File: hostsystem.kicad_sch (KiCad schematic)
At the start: 78 parts, among them J1001 TC2050, J1002 Conn_01x03_Pin, U1001 AM6231ASGGGAALW, U1002 SN74LVC2G241DCUR, U1003 AT24C32D-STUM-T, X1001 32.768kHz, X1002 25MHz

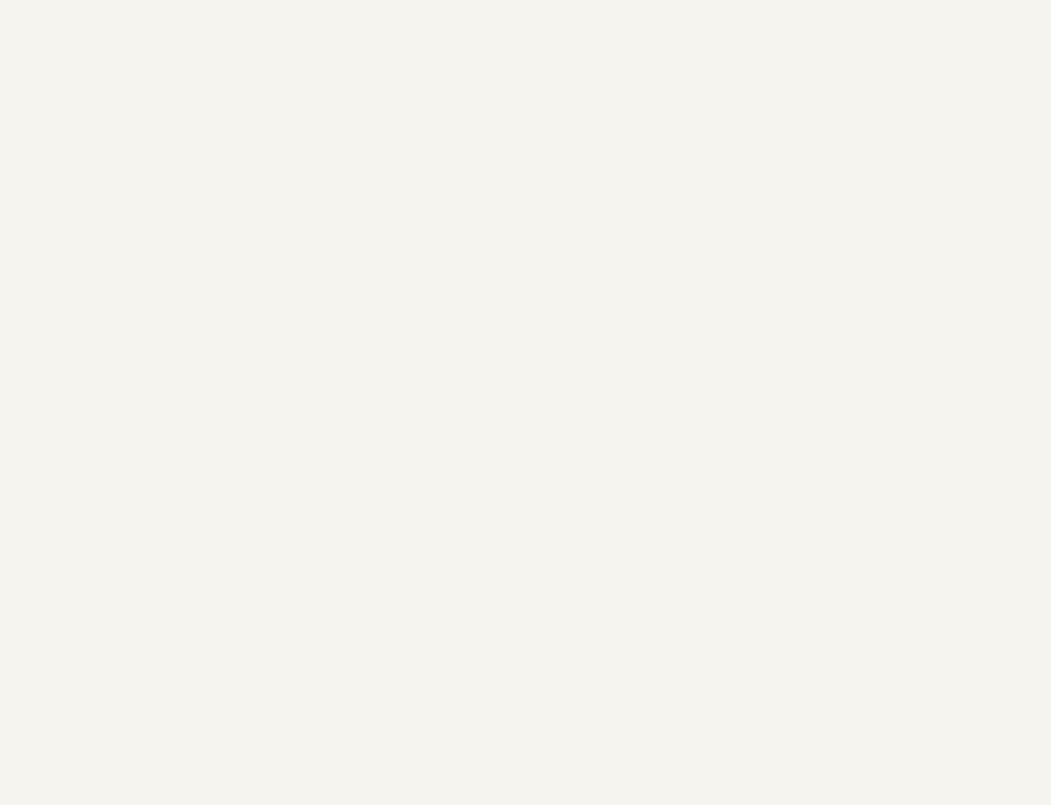
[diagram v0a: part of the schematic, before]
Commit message: Added clock buffor for CMOS 25MHz osc. Used for both SoC and Ethernet with optional SoC crystal still placed
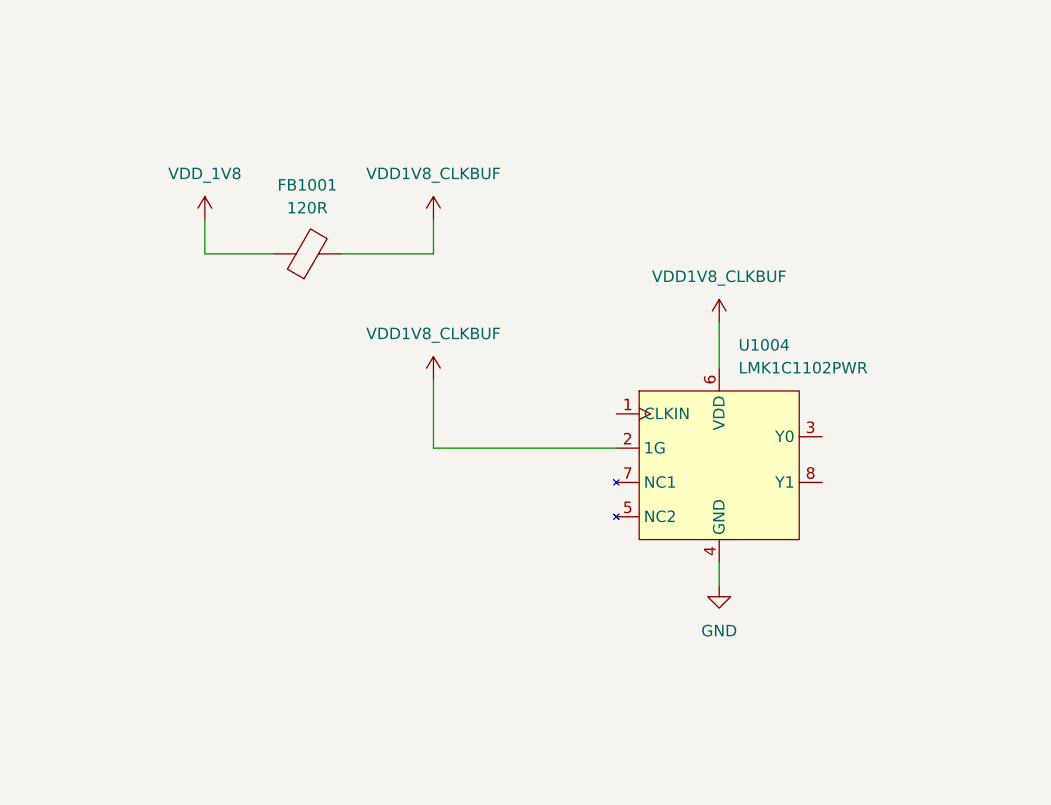
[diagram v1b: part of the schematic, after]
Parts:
- added FB1001: 120R, symbol Device:FerriteBead
- added U1004: LMK1C1102PWR, symbol SoftServicesSymbolLibrary:LMK1C1102PWR
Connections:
- net GND: now also U1004.4 (GND)
- net VDD_1V8: now also FB1001.1
- new net VDD1V8_CLKBUF: FB1001.2, U1004.2 (1G), U1004.6 (VDD)

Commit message: Started USB and OSC routing
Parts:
- removed C1008, C1009: C, Capacitor_SMD:C_0402_1005Metric, symbol Device:C
- removed R1012: 0R, Resistor_SMD:R_0402_1005Metric, symbol Device:R
- added C1010: 0.01u, Capacitor_SMD:C_0201_0603Metric, symbol Device:C
- added C1011: 1u, symbol Device:C
- added C1012, C1013: 0.1u, symbol Device:C
- added R1015: 10k, symbol Device:R
- added R1056, R1057, R1058: 22R, symbol Device:R
- added R1059, R1060: R, symbol Device:R
- added R1061, R1062: 0R, symbol Device:R
- added X1004: ECS-2520MV-250-CN-TR, ECS-2520MV-250-CN-TR:ECS2520MV250CNTR, symbol SoftServicesSymbolLibrary:ECS-2520MV-250-CN-TR
- U1004: footprint (none) -> LMK1C1102PWR:SOP65P640X120-8N
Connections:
- net MCU_OSC0 is gone; now on net MCU_OSC0_XO: U1001.A3 (MCU_SPI0_OSC0_XO)
- net GND: now also C1010.2, C1011.2, C1012.2, C1013.2, R1062.1, X1004.2 (GND)
- net MCU_OSC0_XI: now also R1059.1, R1061.1; no longer C1004.1, X1002.3
- net MCU_OSC0_XO: now also R1060.1, R1062.2; no longer C1006.1, X1002.1
- net VDD1V8_CLKBUF: now also C1010.1, C1011.1, C1012.1, C1013.1, R1015.1, X1004.1 (EN), X1004.4 (VDD); no longer U1004.2 (1G)
- net CLKOUT: now reaches U1004.1 (CLKIN)
- net CLKOUT: now also R1058.2
- net SoC_CLK_BUF: now reaches U1004.3 (Y0)
- net SoC_CLK_BUF: now also R1056.1
- net ETH_CLK_BUF: now reaches U1004.8 (Y1)
- net ETH_CLK_BUF: now also R1057.1
- new net: C1004.1, R1059.2, X1002.3
- new net: C1006.1, R1060.2, X1002.1
- new net CLKBUF_1G: R1015.2, U1004.2 (1G)
- new net CLKOUT_OSC: R1058.1, X1004.3 (OUT)
- new net ETH_CLK: R1057.2
- new net SoC_CLKIN: R1056.2, R1061.2
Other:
- moved on the sheet: C1004, C1006, U1004, X1002

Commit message: Routed most of Ethernet PHY and RGMII
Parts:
- R1015, R1056, R1057, R1058: footprint (none) -> Resistor_SMD:R_0201_0603Metric
- R1061, R1062: footprint (none) -> Resistor_SMD:R_0402_1005Metric
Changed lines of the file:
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@@
 			)
 		)
-		(property "Footprint" ""
+		(property "Footprint" "Resistor_SMD:R_0402_1005Metric"
 			(at 193.04 208.788 90)
 			(effects
@@
 			)
 		)
-		(property "Footprint" ""
+		(property "Footprint" "Resistor_SMD:R_0201_0603Metric"
 			(at 344.932 124.46 90)
 			(effects
@@
 			)
 		)
-		(property "Footprint" ""
+		(property "Footprint" "Resistor_SMD:R_0201_0603Metric"
 			(at 321.31 131.318 90)
 			(effects
@@
 			)
 		)
-		(property "Footprint" ""
+		(property "Footprint" "Resistor_SMD:R_0201_0603Metric"
 			(at 408.94 135.128 90)
 			(effects
@@
 			)
 		)
-		(property "Footprint" ""
+		(property "Footprint" "Resistor_SMD:R_0402_1005Metric"
 			(at 185.928 254 90)
 			(effects
@@
 			)
 		)
-		(property "Footprint" ""
+		(property "Footprint" "Resistor_SMD:R_0201_0603Metric"
 			(at 408.94 130.048 90)
 			(effects

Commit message: Continued PDN routing
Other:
- note added: "CMOS Oscillator + Clock Buffer"
- moved on the sheet: D1004, D1005, D1006, FB1001, R1016, R1017, R1018, R1019, R1020, R1021, R1022, R1023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

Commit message: Improved clock layout and clock PDN
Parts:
- C1010: footprint Capacitor_SMD:C_0201_0603Metric -> Capacitor_SMD:C_0402_1005Metric
- C1011, C1012, C1013: footprint (none) -> Capacitor_SMD:C_0402_1005Metric
- FB1001: footprint (none) -> Resistor_SMD:R_0402_1005Metric
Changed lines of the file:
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@@
 			)
 		)
-		(property "Footprint" "Capacitor_SMD:C_0201_0603Metric"
+		(property "Footprint" "Capacitor_SMD:C_0402_1005Metric"
 			(at 263.8552 132.08 0)
 			(effects
@@
 			)
 		)
-		(property "Footprint" ""
+		(property "Footprint" "Capacitor_SMD:C_0402_1005Metric"
 			(at 229.5652 154.94 0)
 			(effects
@@
 			)
 		)
-		(property "Footprint" ""
+		(property "Footprint" "Resistor_SMD:R_0402_1005Metric"
 			(at 228.6 130.048 90)
 			(effects
@@
 			)
 		)
-		(property "Footprint" ""
+		(property "Footprint" "Capacitor_SMD:C_0402_1005Metric"
 			(at 215.5952 154.94 0)
 			(effects
@@
 			)
 		)
-		(property "Footprint" ""
+		(property "Footprint" "Capacitor_SMD:C_0402_1005Metric"
 			(at 243.5352 154.94 0)
 			(effects

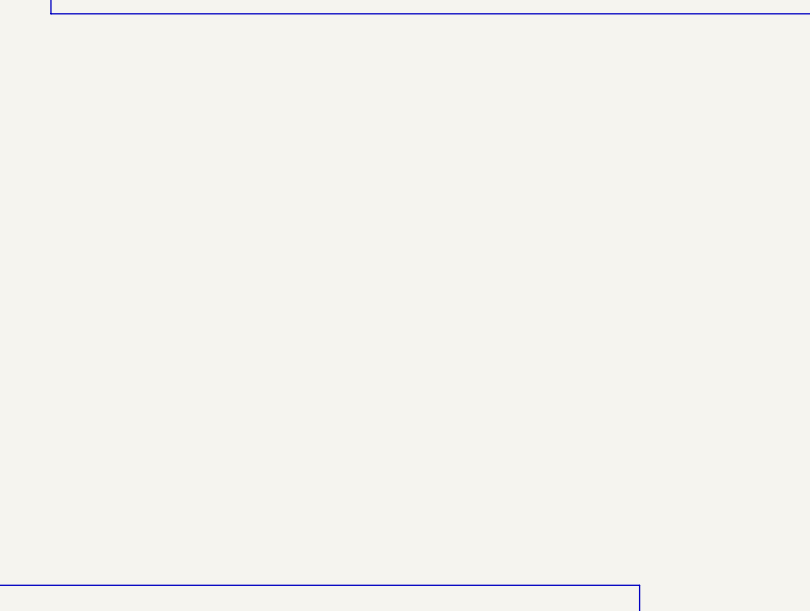
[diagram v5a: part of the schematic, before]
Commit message: Switched out CC2652P and nRF52840 for MGM240P to run Zigbee and Thread
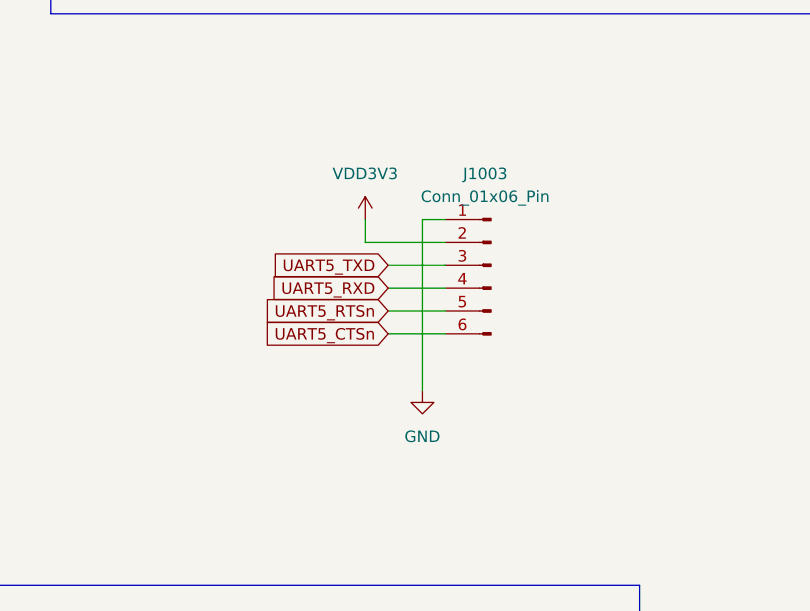
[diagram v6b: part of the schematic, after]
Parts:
- added J1003: Conn_01x06_Pin, Connector_PinHeader_2.54mm:PinHeader_1x06_P2.54mm_Vertical, symbol Connector:Conn_01x06_Pin
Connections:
- net GND: now also J1003.1 (Pin_1)
- net UART5_CTSn: now also J1003.6 (Pin_6)
- net UART5_RTSn: now also J1003.5 (Pin_5)
- net UART5_RXD: now also J1003.4 (Pin_4)
- net UART5_TXD: now also J1003.3 (Pin_3)
- new net VDD3V3: J1003.2 (Pin_2)

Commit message: Added new radio schematic
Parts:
- removed R1054: 100R, symbol Device:R
- removed R1055: 100k, symbol Device:R
- R1046: renamed from R1011; value 33R -> 22R
- R1049: renamed from R1052; value 33R -> 22R
- R1051: renamed from R1053; value 33R -> 22R
- renumbered C1010 to C1001, C1011 to C1002, C1012 to C1003, C1013 to C1004, C1004 to C1005, C1002 to C1007, C1003 to C1008, C1001 to C1009, C1007 to C1010, C1005 to C1011, D1004 to D1001, D1005 to D1002, D1006 to D1003, D1001 to D1004, D1002 to D1005, D1003 to D1006, J1003 to J1001, J1001 to J1002, J1002 to J1003, R1048 to R1001, R1016 to R1002, R1017 to R1003, R1018 to R1004, R1019 to R1005, R1020 to R1006, R1021 to R1007, R1023 to R1008, R1022 to R1009, R1024 to R1010, R1025 to R1011, R1026 to R1012, R1027 to R1013, R1028 to R1014, R1029 to R1015, R1030 to R1016, R1031 to R1017, R1001 to R1018, R1002 to R1019, R1015 to R1020, R1056 to R1021, R1058 to R1022, R1057 to R1023, R1049 to R1024, R1050 to R1025, R1051 to R1026, R1032 to R1027, R1033 to R1028, R1034 to R1029, R1035 to R1030, R1036 to R1031, R1037 to R1032, R1038 to R1033, R1039 to R1034, R1040 to R1035, R1041 to R1036, R1042 to R1037, R1043 to R1038, R1044 to R1039, R1045 to R1040, R1046 to R1041, R1047 to R1042, R1009 to R1043, R1010 to R1044, R1061 to R1045, R1059 to R1047, R1060 to R1052, R1062 to R1053, R1003 to R1054, R1004 to R1055, R1005 to R1056, R1006 to R1057, R1007 to R1058, R1013 to R1059, R1014 to R1060, R1008 to R1061, U1004 to U1001, U1001 to U1002, U1002 to U1003, U1003 to U1004, X1004 to X1001, X1001 to X1003
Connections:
- net CC2652_BOOT: no longer names the net of U1002.F23 (OSPI0_CSN0)
- net CC2652_RSTn: no longer names the net of U1002.G21 (OSPI0_CSN1)
- net CC2652_UART6_CTSn: no longer names the net of U1002.J22 (OSPI0_D7)
- net CC2652_UART6_RTSn: no longer names the net of U1002.H25 (OSPI0_D6)
- net CC2652_UART6_RXD: no longer names the net of U1002.J23 (OSPI0_D4)
- net CC2652_UART6_TXD: no longer names the net of U1002.J25 (OSPI0_D5)
- net nRF_INTn renamed MDM_SPI0_IRQ
- net nRF_SPI0_CLK renamed MGM_SPI0_CLK
- net nRF_SPI0_CS0 renamed MGM_SPI0_CS
- net nRF_SPI0_MISO renamed MGM_SPI0_MISO
- net nRF_SPI0_MOSI renamed MGM_SPI0_MOSI
- net nRF_SoC_CLK renamed MGM_SoC_CLK
- net nRF_SoC_MOSI renamed MGM_SoC_MOSI
- net nRF_SoC_nRESET: no longer names the net of U1002.B15 (UART0_RTSN)
- no-connect marks 103 -> 109

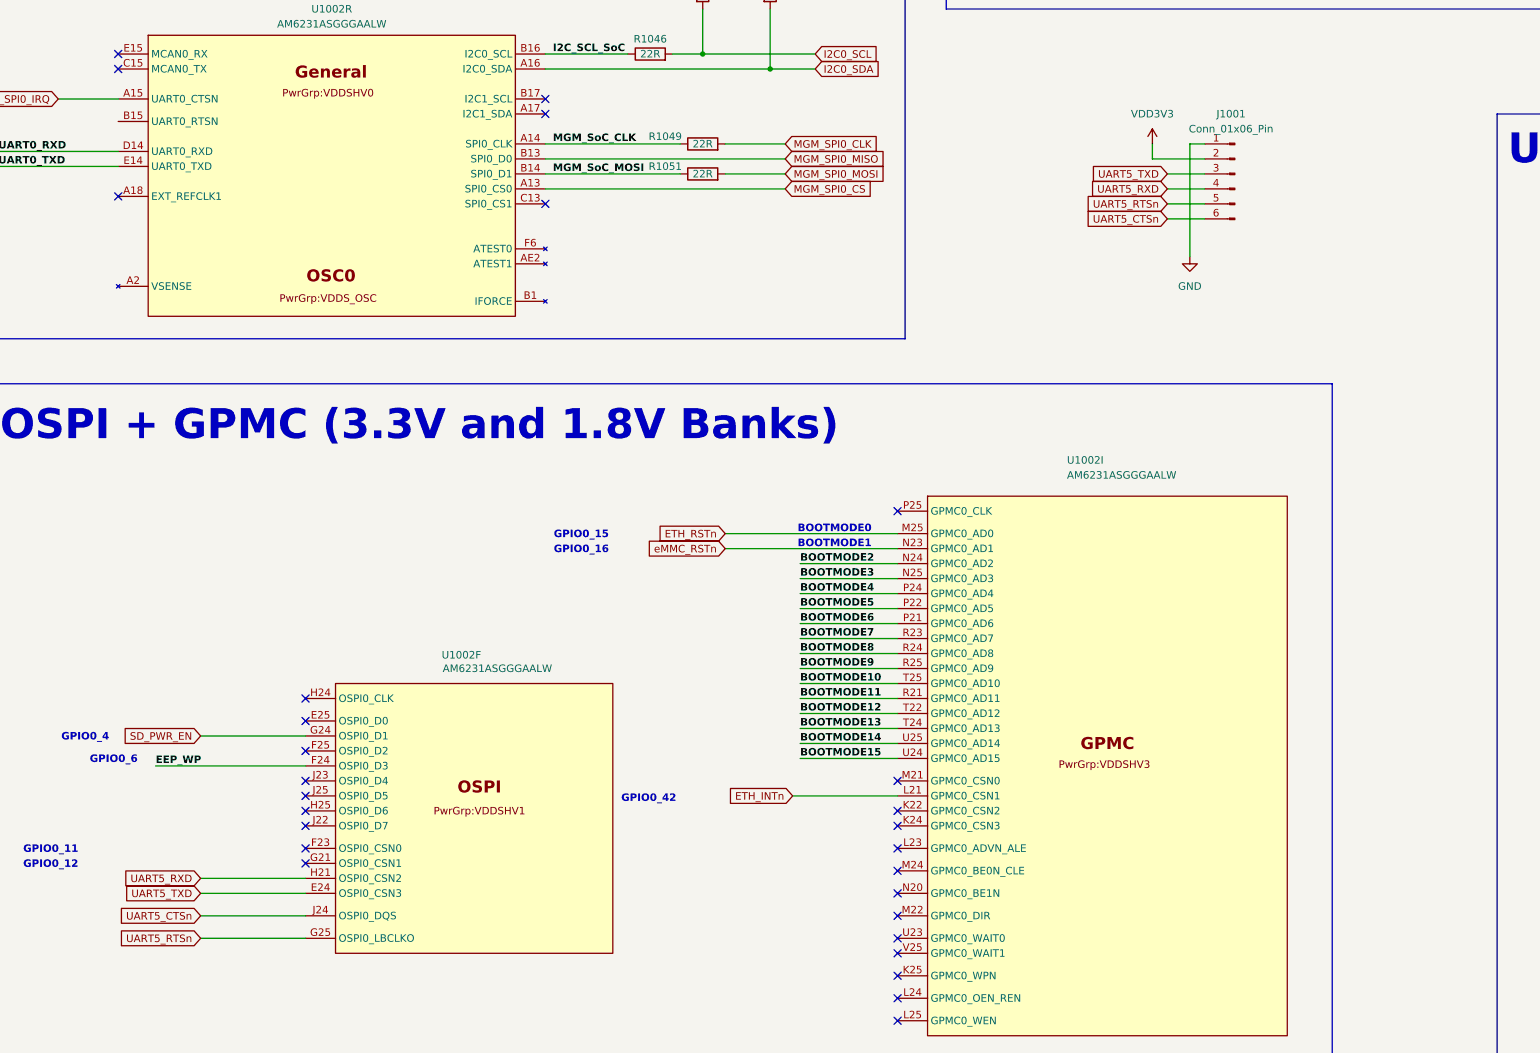
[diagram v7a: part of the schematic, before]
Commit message: Added UART and SPI header pins for MGM240P module options
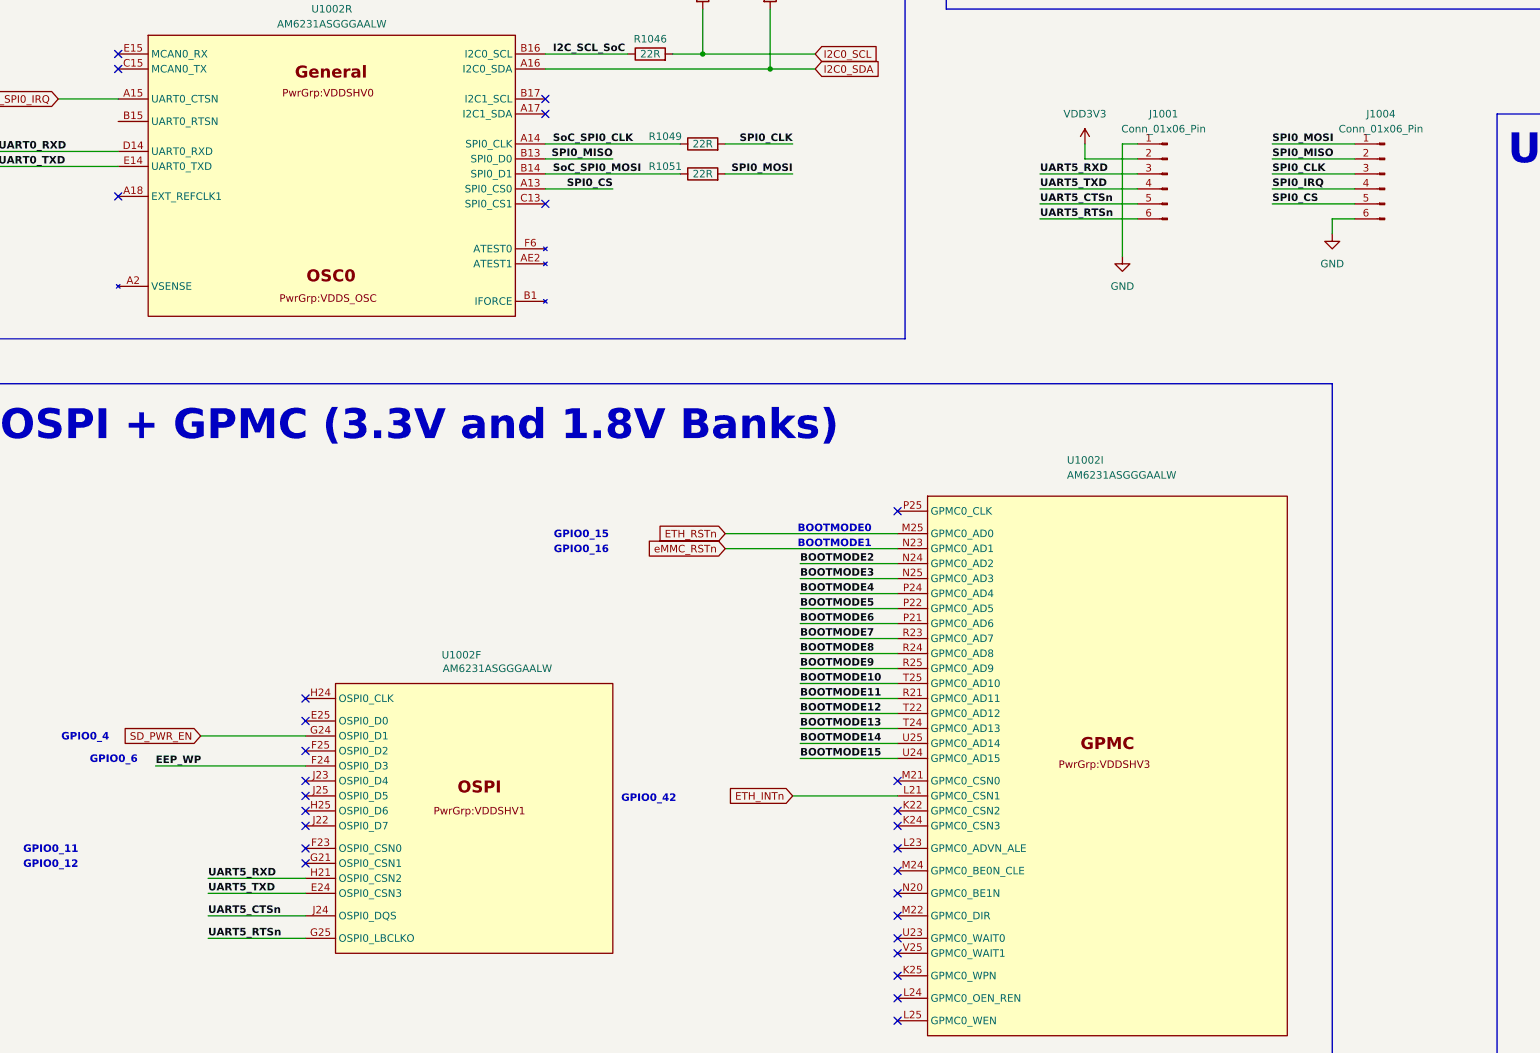
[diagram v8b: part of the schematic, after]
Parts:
- added J1004: Conn_01x06_Pin, Connector_PinHeader_2.54mm:PinHeader_1x06_P2.54mm_Vertical, symbol Connector:Conn_01x06_Pin
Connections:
- net GND: now also J1004.6 (Pin_6)
- net UART5_CTSn: now also J1001.5 (Pin_5); no longer J1001.6 (Pin_6)
- net UART5_RTSn: now also J1001.6 (Pin_6); no longer J1001.5 (Pin_5)
- net UART5_RXD: now also J1001.3 (Pin_3); no longer J1001.4 (Pin_4)
- net UART5_TXD: now also J1001.4 (Pin_4); no longer J1001.3 (Pin_3)
- net MGM_SPI0_CLK renamed SPI0_CLK
- net SPI0_CLK: now also J1004.3 (Pin_3)
- net MGM_SPI0_CS renamed SPI0_CS
- net SPI0_CS: now also J1004.5 (Pin_5)
- net MGM_SPI0_MISO renamed SPI0_MISO
- net SPI0_MISO: now also J1004.2 (Pin_2)
- net MGM_SPI0_MOSI renamed SPI0_MOSI
- net SPI0_MOSI: now also J1004.1 (Pin_1)
- net MGM_SoC_CLK renamed SoC_SPI0_CLK
- net MGM_SoC_MOSI renamed SoC_SPI0_MOSI
- new net SPI0_IRQ: J1004.4 (Pin_4)
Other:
- moved on the sheet: J1001
